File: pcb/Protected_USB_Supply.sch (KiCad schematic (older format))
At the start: 6 parts, among them P2 USB, U7 USBLC6-2SC6

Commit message: Fix some assignment problems because of wrong library/component names
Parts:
- P2: footprint Connect:USB_Micro-B_10103594-0001LF -> Connectors:USB_Micro-B_10103594-0001LF
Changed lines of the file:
@@
 F 0 "P2" V 3875 3424 50  0000 C CNN
 F 1 "USB" V 3966 3424 50  0000 C CNN
-F 2 "Connect:USB_Micro-B_10103594-0001LF" V 4250 3400 50  0001 C CNN
+F 2 "Connectors:USB_Micro-B_10103594-0001LF" V 4250 3400 50  0001 C CNN
 F 3 "" V 4250 3400 50  0000 C CNN
 	1    4300 3500

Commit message: Add some digikey order informations to components
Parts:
- P2: Digi-Key Minimum Quantity (none) -> 1; Digi-Key Part Number (none) -> 609-4050-1-ND
- U7: Digi-Key Minimum Quantity (none) -> 1; Digi-Key Part Number (none) -> 497-5235-1-ND
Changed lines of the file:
@@
 F 1 "USBLC6-2SC6" H 5500 3074 50  0000 C CNN
 F 2 "TO_SOT_Packages_SMD:SOT-23-6" H 6150 3800 50  0001 C CNN
-F 3 "" H 5250 3800 50  0001 C CNN
+F 3 "http://www.st.com/content/ccc/resource/technical/document/datasheet/06/1d/48/9c/6c/20/4a/b2/CD00050750.pdf/files/CD00050750.pdf/jcr:content/translations/en.CD00050750.pdf" H 5250 3800 50  0001 C CNN
+F 4 "497-5235-1-ND" H 5500 3450 60  0001 C CNN "Digi-Key Part Number"
+F 5 "1" H 5500 3450 60  0001 C CNN "Digi-Key Minimum Quantity"
 	1    5500 3450
 	1    0    0    1
@@
 F 1 "USB" V 3966 3424 50  0000 C CNN
 F 2 "Connectors:USB_Micro-B_10103594-0001LF" V 4250 3400 50  0001 C CNN
-F 3 "" V 4250 3400 50  0000 C CNN
+F 3 "http://portal.fciconnect.com/Comergent//fci/drawing/10103594.pdf" V 4250 3400 50  0001 C CNN
+F 4 "609-4050-1-ND" V 4300 3500 60  0001 C CNN "Digi-Key Part Number"
+F 5 "1" V 4300 3500 60  0001 C CNN "Digi-Key Minimum Quantity"
 	1    4300 3500
 	0    -1   1    0

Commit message: Add more BOM informations
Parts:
- C29: Digi-Key Minimum Quantity (none) -> 1; Digi-Key Part Number (none) -> 311-1343-1-ND
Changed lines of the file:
@@
 F 2 "Capacitors_SMD:C_0603" H 5538 3950 50  0001 C CNN
 F 3 "" H 5500 4100 50  0000 C CNN
+F 4 "311-1343-1-ND" H 5500 4100 60  0001 C CNN "Digi-Key Part Number"
+F 5 "1" H 5500 4100 60  0001 C CNN "Digi-Key Minimum Quantity"
 	1    5500 4100
 	0    -1   -1   0

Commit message: Improve BOM
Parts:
- F2: Digi-Key Minimum Quantity (none) -> 1; Digi-Key Part Number (none) -> 507-1802-1-ND
- L2, L3: Digi-Key Minimum Quantity (none) -> 1; Digi-Key Part Number (none) -> MH1608-471YCT-ND
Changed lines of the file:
@@
 F 1 "FERRIT_BEAD" H 4247 4055 50  0000 L CNN
 F 2 "Resistors_SMD:R_0603" H 4200 4100 50  0001 C CNN
-F 3 "" H 4200 4100 50  0000 C CNN
+F 3 "http://www.bourns.com/docs/Product-Datasheets/mh.pdf" H 4200 4100 50  0001 C CNN
+F 4 "MH1608-471YCT-ND" H 4200 4100 60  0001 C CNN "Digi-Key Part Number"
+F 5 "1" H 4200 4100 60  0001 C CNN "Digi-Key Minimum Quantity"
 	1    4200 4100
 	1    0    0    -1
@@
 F 1 "500mA" V 6249 2900 50  0000 C CNN
 F 2 "Resistors_SMD:R_1206" H 6400 2900 50  0001 C CNN
-F 3 "" H 6400 2900 50  0000 C CNN
+F 3 "http://www.belfuse.com/pdfs/0ZCJ.pdf" H 6400 2900 50  0001 C CNN
+F 4 "507-1802-1-ND" H 6400 2900 60  0001 C CNN "Digi-Key Part Number"
+F 5 "1" H 6400 2900 60  0001 C CNN "Digi-Key Minimum Quantity"
 	1    6400 2900
 	0    1    1    0
@@
 F 1 "FERRIT_BEAD" V 6894 2900 50  0000 C CNN
 F 2 "Resistors_SMD:R_0603" H 6800 2900 50  0001 C CNN
-F 3 "" H 6800 2900 50  0000 C CNN
+F 3 "http://www.bourns.com/docs/Product-Datasheets/mh.pdf" H 6800 2900 50  0001 C CNN
+F 4 "MH1608-471YCT-ND" H 6800 2900 60  0001 C CNN "Digi-Key Part Number"
+F 5 "1" H 6800 2900 60  0001 C CNN "Digi-Key Minimum Quantity"
 	1    6800 2900
 	0    -1   -1   0

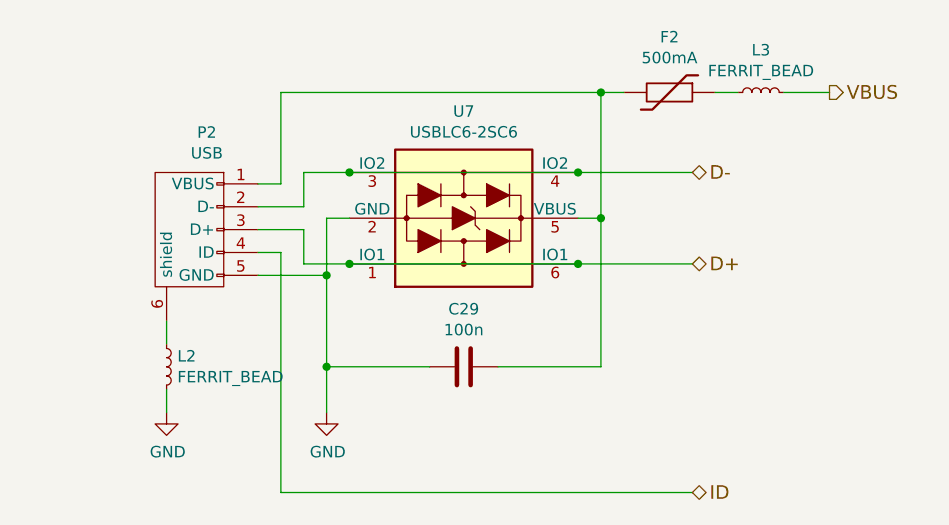
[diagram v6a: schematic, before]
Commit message: Use new library symbols
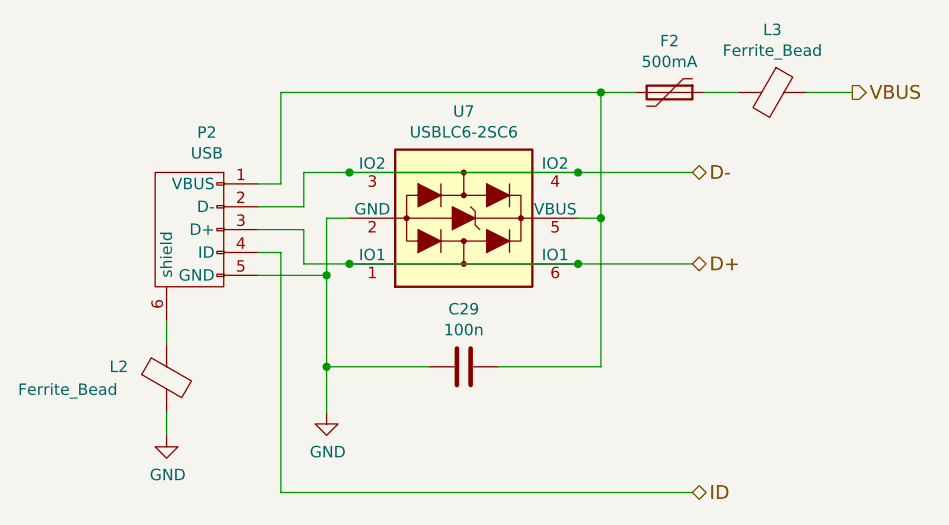
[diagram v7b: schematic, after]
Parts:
- removed F2: 500mA, Resistors_SMD:R_1206, symbol THERMISTOR
- removed L2, L3: FERRIT_BEAD, Resistors_SMD:R_0603, symbol INDUCTOR_Small
- added F2: 500mA, Resistors_SMD:R_1206, symbol Polyfuse
- added L2, L3: Ferrite_Bead, Resistors_SMD:R_0603, symbol Ferrite_Bead
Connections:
- net GND: now also L2.2
- net VBUS: now also L3.1
- net at C29.2, P2.1 (VBUS), U7.5 (VBUS): now also F2.2
- net at P2.6 (shield): now also L2.1
- new net: F2.1, L3.2
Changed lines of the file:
@@
 	0    -1   1    0
-$EndComp
-$Comp
-L INDUCTOR_Small L2
-U 1 1 580C1770
-P 4200 4100
-F 0 "L2" H 4247 4146 50  0000 L CNN
-F 1 "FERRIT_BEAD" H 4247 4055 50  0000 L CNN
-F 2 "Resistors_SMD:R_0603" H 4200 4100 50  0001 C CNN
-F 3 "http://www.bourns.com/docs/Product-Datasheets/mh.pdf" H 4200 4100 50  0001 C CNN
-F 4 "MH1608-471YCT-ND" H 4200 4100 60  0001 C CNN "Digi-Key Part Number"
-F 5 "1" H 4200 4100 60  0001 C CNN "Digi-Key Minimum Quantity"
-	1    4200 4100
-	1    0    0    -1
 $EndComp
 Wire Wire Line
@@
 L GND #PWR082
 U 1 1 580C1786
-P 4200 4300
-F 0 "#PWR082" H 4200 4050 50  0001 C CNN
-F 1 "GND" H 4205 4127 50  0000 C CNN
-F 2 "" H 4200 4300 50  0000 C CNN
-F 3 "" H 4200 4300 50  0000 C CNN
-	1    4200 4300
+P 4200 4400
+F 0 "#PWR082" H 4200 4150 50  0001 C CNN
+F 1 "GND" H 4205 4227 50  0000 C CNN
+F 2 "" H 4200 4400 50  0000 C CNN
+F 3 "" H 4200 4400 50  0000 C CNN
+	1    4200 4400
 	1    0    0    -1
 $EndComp
@@
 	4200 3900 4200 4000
 Wire Wire Line
-	4200 4200 4200 4300
+	4200 4300 4200 4400
 Wire Wire Line
-	4700 2900 6200 2900
+	4700 2900 6250 2900
 Wire Wire Line
 	6100 2900 6100 4100
@@
 Wire Wire Line
 	4700 3300 4600 3300
-$Comp
-L THERMISTOR F2
-U 1 1 580C1793
-P 6400 2900
-F 0 "F2" V 6158 2900 50  0000 C CNN
-F 1 "500mA" V 6249 2900 50  0000 C CNN
-F 2 "Resistors_SMD:R_1206" H 6400 2900 50  0001 C CNN
-F 3 "http://www.belfuse.com/pdfs/0ZCJ.pdf" H 6400 2900 50  0001 C CNN
-F 4 "507-1802-1-ND" H 6400 2900 60  0001 C CNN "Digi-Key Part Number"
-F 5 "1" H 6400 2900 60  0001 C CNN "Digi-Key Minimum Quantity"
-	1    6400 2900
-	0    1    1    0
-$EndComp
-$Comp
-L INDUCTOR_Small L3
-U 1 1 580C179A
-P 6800 2900
-F 0 "L3" V 6985 2900 50  0000 C CNN
-F 1 "FERRIT_BEAD" V 6894 2900 50  0000 C CNN
-F 2 "Resistors_SMD:R_0603" H 6800 2900 50  0001 C CNN
-F 3 "http://www.bourns.com/docs/Product-Datasheets/mh.pdf" H 6800 2900 50  0001 C CNN
-F 4 "MH1608-471YCT-ND" H 6800 2900 60  0001 C CNN "Digi-Key Part Number"
-F 5 "1" H 6800 2900 60  0001 C CNN "Digi-Key Minimum Quantity"
-	1    6800 2900
-	0    -1   -1   0
-$EndComp
 $Comp
 L C C29
@@
 Connection ~ 6100 2900
 Wire Wire Line
-	6700 2900 6600 2900
+	6550 2900 6700 2900
 Wire Wire Line
-	6900 2900 7100 2900
+	7000 2900 7200 2900
 Text HLabel 6500 3250 2    60   BiDi ~ 0
 D-
 Text HLabel 6500 3650 2    60   BiDi ~ 0
 D+
-Text HLabel 7100 2900 2    60   Output ~ 0
+Text HLabel 7200 2900 2    60   Output ~ 0
 VBUS
 Wire Wire Line
@@
 Text HLabel 6500 4650 2    60   BiDi ~ 0
 ID
+$Comp
+L Polyfuse F2
+U 1 1 582EA403
+P 6400 2900
+F 0 "F2" V 6175 2900 50  0000 C CNN
+F 1 "500mA" V 6266 2900 50  0000 C CNN
+F 2 "Resistors_SMD:R_1206" H 6450 2700 50  0001 L CNN
+F 3 "http://www.belfuse.com/pdfs/0ZCJ.pdf" H 6400 2900 50  0001 C CNN
+F 4 "507-1802-1-ND" H 6400 2900 60  0001 C CNN "Digi-Key Part Number"
+F 5 "1" H 6400 2900 60  0001 C CNN "Digi-Key Minimum Quantity"
+	1    6400 2900
+	0    1    1    0
+$EndComp
+$Comp
+L Ferrite_Bead L3
+U 1 1 582EAA94
+P 6850 2900
+F 0 "L3" V 6576 2900 50  0000 C CNN
+F 1 "Ferrite_Bead" V 6667 2900 50  0000 C CNN
+F 2 "Resistors_SMD:R_0603" V 6668 2900 50  0001 C CNN
+F 3 "http://www.bourns.com/docs/Product-Datasheets/mh.pdf" V 6667 2900 50  0001 C CNN
+F 4 "MH1608-471YCT-ND" H 6850 2900 60  0001 C CNN "Digi-Key Part Number"
+F 5 "1" H 6850 2900 60  0001 C CNN "Digi-Key Minimum Quantity"
+	1    6850 2900
+	0    1    1    0
+$EndComp
+$Comp
+L Ferrite_Bead L2
+U 1 1 582EB03B
+P 4200 4150
+F 0 "L2" H 3950 4200 50  0000 L CNN
+F 1 "Ferrite_Bead" H 3550 4100 50  0000 L CNN
+F 2 "Resistors_SMD:R_0603" V 4018 4150 50  0001 C CNN
+F 3 "http://www.bourns.com/docs/Product-Datasheets/mh.pdf" V 4017 4150 50  0001 C CNN
+F 4 "MH1608-471YCT-ND" H 4200 4150 60  0001 C CNN "Digi-Key Part Number"
+F 5 "1" H 4200 4150 60  0001 C CNN "Digi-Key Minimum Quantity"
+	1    4200 4150
+	1    0    0    -1
+$EndComp
 $EndSCHEMATC
